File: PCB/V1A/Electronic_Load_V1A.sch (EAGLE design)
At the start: 209 parts, among them IC101 LM50, IC102 LM50, IC301 7805T, IC302 OPA77P, Q101 SIRC10DP, Q102 SIRC10DP, Q103 BC817-16SMD, Q104 BC817-16SMD, Q105 BC807-16SMD, Q106 SIRC10DP, Q107 IXTK102N65X2R+, Q108 SIRC10DP, Q109 SIRC10DP, Q110 SIRC10DP, Q111 IXTK102N65X2R+, Q601 BC807-16SMD, Q602 BC807-16SMD, Q603 BC807-16SMD, Q604 BC807-16SMD, Q605 BC807-16SMD, Q606 BC807-16SMD, Q607 BC807-16SMD, Q608 BC807-16SMD, Q609 BC807-16SMD, Q610 BC807-16SMD, Q611 BC807-16SMD, Q612 BC807-16SMD, U101 AD420, U102 AD420, U103 LT1014I, U104 LTC1865L, U201 AD620, U202 AD620, U203 AD620, U204 AD620, U205 AD620, U206 LTC1865L, U207 LTC1865L, U208 LTC1865L, U301 MAX743, U601 HCPL-063N, U602 HCPL-063N, U603 HCPL-063N, U604 HCPL-063N, U605 HCPL-063N, U606 HCPL-063N

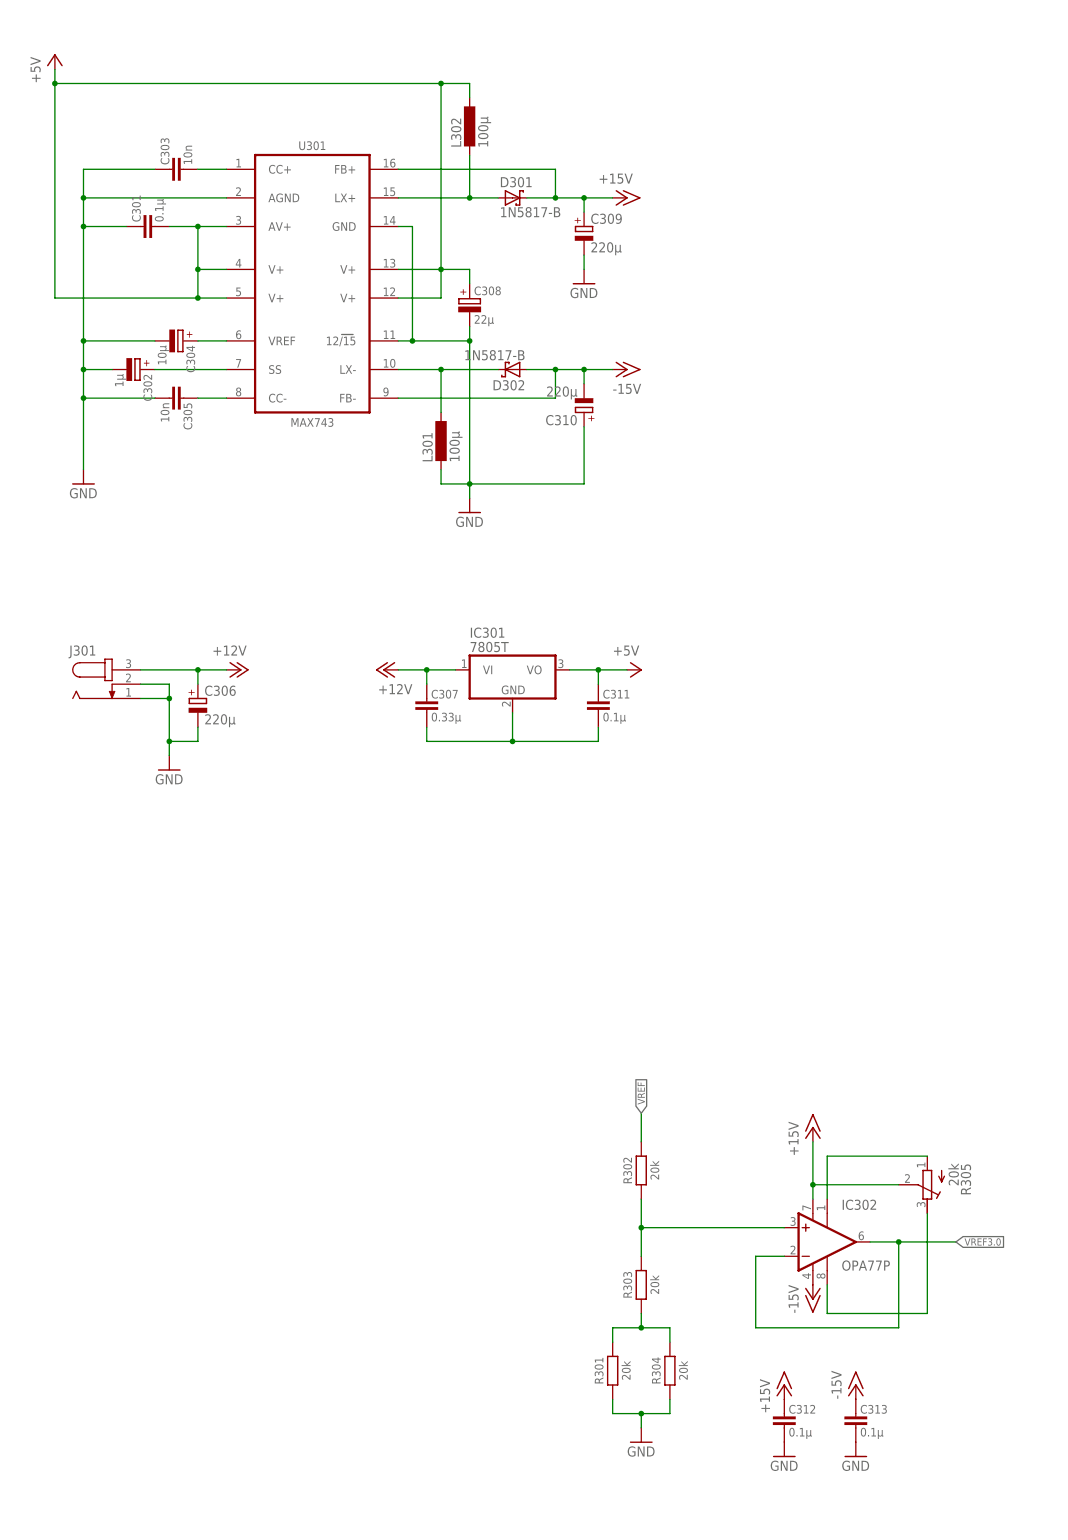
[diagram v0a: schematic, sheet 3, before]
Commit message: ADC/DAC board layout
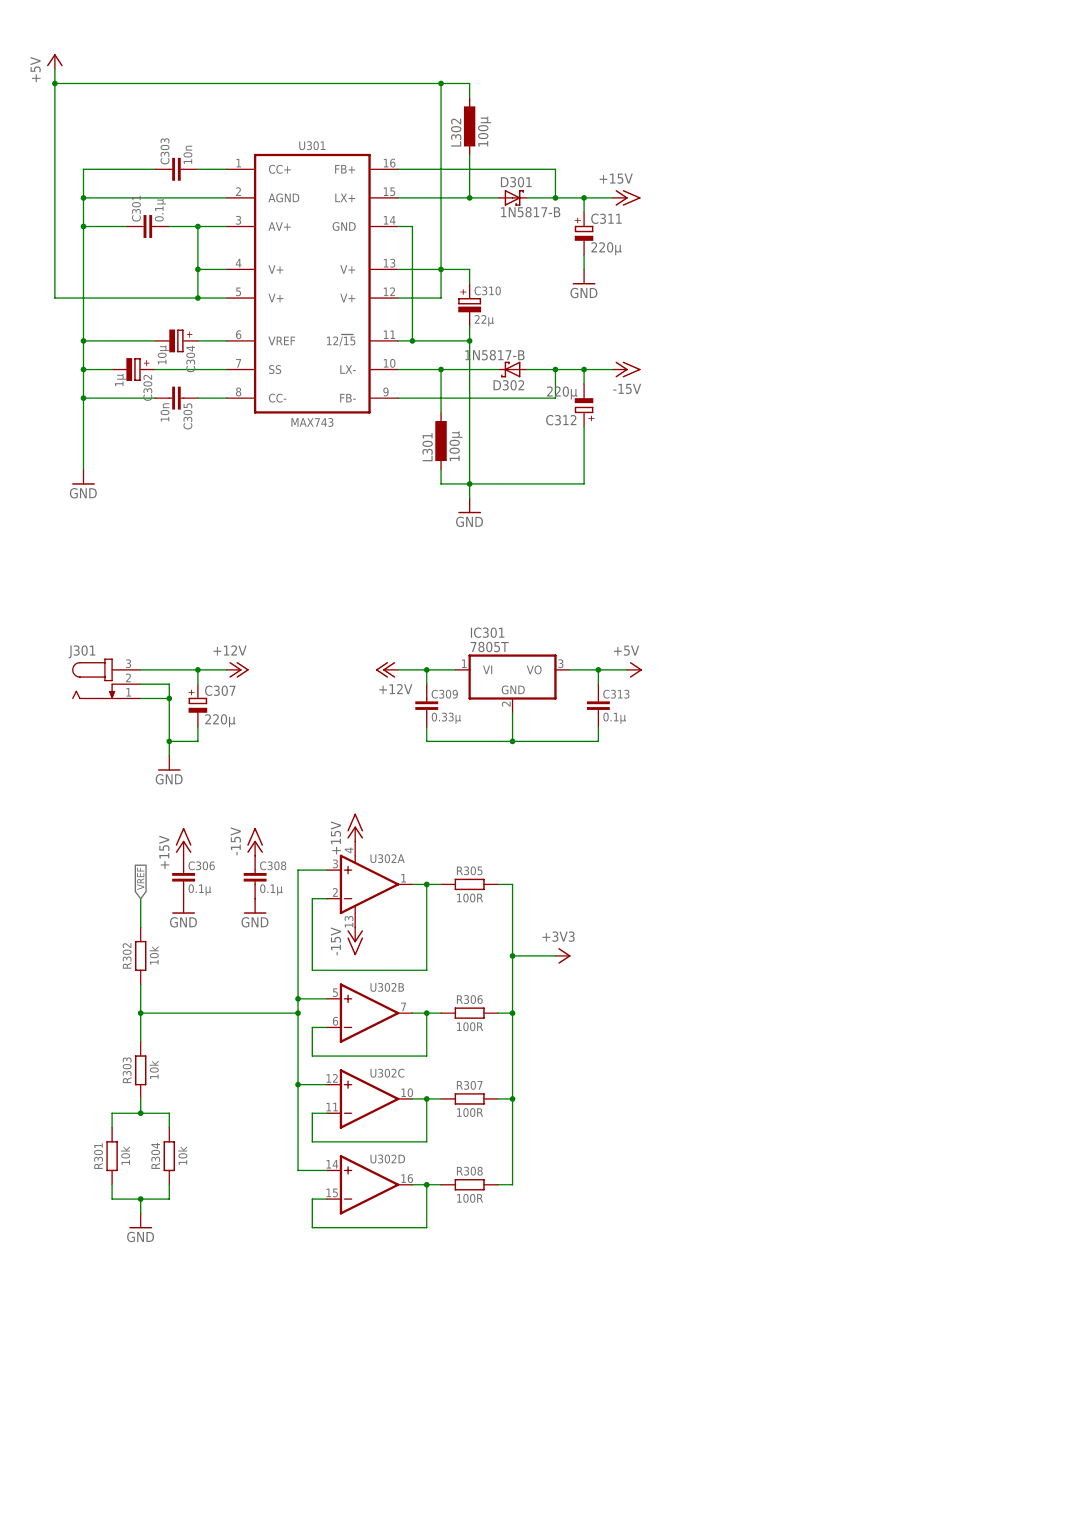
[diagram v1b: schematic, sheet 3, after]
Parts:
- removed IC302: OPA77P, burr-brown:OPA77P
- added R306, R307, R308: 100R, passives:R-EU-3225
- added U302: (no value), ic:LT1014ISW
- C306: value 220µ -> 0.1µ; device rcl:CPOL-EUE3.5-10 -> passives:C-EU-3216
- C307: value 0.33µ -> 220µ; device passives:C-EU-3216 -> rcl:CPOL-EUE3.5-10
- C308: value 22µ -> 0.1µ; device passives:CPOL-6032-C -> passives:C-EU-3216
- C309: value 220µ -> 0.33µ; device rcl:CPOL-EUE3.5-10 -> passives:C-EU-3216
- C310: value 220µ -> 22µ; device rcl:CPOL-EUE3.5-10 -> passives:CPOL-6032-C
- C311, C312: value 0.1µ -> 220µ; device passives:C-EU-3216 -> rcl:CPOL-EUE3.5-10
- R301, R302, R303, R304: value 20k -> 10k
- R305: value 20k -> 100R; device rcl:R-TRIMM4G/J -> passives:R-EU-3225
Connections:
- removed net BYP_G_LOL: Q604.B
- removed net DAC_CLR_ISO: C609.1, R609.1, U603.VO1
- removed net N$78: IC302.+IN, R302.1, R303.2
- removed net N$80: IC302.TRIM2, R305.E
- removed net N$81: IC302.TRIM1, R305.A
- removed net VREF3.0: IC302.-IN, IC302.OUT
- new net BYP: Q603.B
- new net CLR_DAC: Q601.B
- new net N$37: R302.1, R303.2, U302A.+IN, U302B.+IN, U302C.+IN, U302D.+IN
- new net N$38: R306.1, U302B.-IN, U302B.OUT
- new net N$39: R305.1, U302A.-IN, U302A.OUT
- new net N$40: R307.1, U302C.-IN, U302C.OUT
- new net N$43: R308.1, U302D.-IN, U302D.OUT
- net +12V: now also C307.+, C309.1; no longer C306.+, C307.1
- net +15V: now also C306.1, C311.+, U302A.V+; no longer C309.+, C312.1, IC302.V+, R305.S
- net +3V3: now also R305.2, R306.2, R307.2, R308.2
- net +5V: now also C310.+, C313.1; no longer C308.+, C311.1
- net -15V: now also C308.1, C312.-, U302A.V-; no longer C310.-, C313.1, IC302.V-
- net BYP_I: now also C609.1, R609.1, U603.VO1; no longer C610.1, R610.1, U601.VO2
- net CLR_DAC_I: now also C607.1, R607.1, U601.VO1; no longer Q603.B
- net GND: now also C306.2, C307.-, C308.2, C310.-, C311.-, C312.+; no longer C306.-, C308.-, C309.-, C310.+, C312.2, C313.2
- net N$42: now also C309.2, C313.2; no longer C307.2, C311.2
- net SS_DAC: now also Q604.B; no longer Q601.B
- net SS_DAC_I: now also C610.1, R610.1, U601.VO2; no longer C607.1, R607.1, U601.VO1
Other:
- moved on the sheet: C310, C313, R301, R302, R303, R304

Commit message: Board layout
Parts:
- added C314: 0.33µ, passives:C-EU-3216
- added C315: 0.1µ, passives:C-EU-3216
- added IC302: 7805T, linear:7805T
- added PAD1, PAD405: S1, pads:PAD-10X4
- added PAD2, PAD406: S2, pads:PAD-10X4
- added PAD3, PAD407: UUT-, pads:PAD-10X4
- added PAD401: G1, pads:PAD-5X2
- added PAD402: G2, pads:PAD-5X2
- added PAD403: VS+, pads:PAD-5X2
- added PAD404: VS-, pads:PAD-5X2
- added R133, R217: 10k, passives:R-EU-1608
- C107: device rcl:C-EUC1206 -> passives:C-EU-1608
- C121, C122, C209, C210, C211, C212, C216, C607, C608, C609, C610, C611, C612, C619, C620, C621, C622, C623, C624: device passives:C-EU-3216 -> passives:C-EU-1608
- R101, R123, R124, R125, R201, R202, R203, R204, R210, R211, R212, R213, R214, R215, R216, R305, R306, R307, R308: device passives:R-EU-3225 -> passives:R-EU-2012
- R102: value 1k -> 10k; device passives:R-EU-3225 -> passives:R-EU-1608
- R103, R107: value 100R -> 1k; device passives:R-EU-3225 -> passives:R-EU-3216
- R104, R115, R120, R126: value 10k -> 100R; device passives:R-EU-3225 -> passives:R-EU-2012
- R105, R114, R119, R122: value 100R -> 10k; device passives:R-EU-3225 -> passives:R-EU-1608
- R106: value 1k -> 100R; device passives:R-EU-3225 -> passives:R-EU-2012
- R108: value 0R004 -> 100R; device rcl:R-EU_R6332 -> passives:R-EU-2012
- R109, R129: value 2R -> 0R004; device passives:R-EU-3225 -> passives:R-EU-6332
- R110, R130: value 0R004 -> 2R; device rcl:R-EU_R6332 -> passives:R-EU-3216
- R111, R131: value 10k -> 0R004; device passives:R-EU-3225 -> passives:R-EU-6332
- R112, R113, R116, R117, R118, R121, R127, R132, R301, R302, R303, R304, R601, R602, R603, R604, R605, R606, R607, R608, R609, R610, R611, R612, R613, R614, R615, R616, R617, R618, R619, R620, R621, R622, R623, R624: device passives:R-EU-3225 -> passives:R-EU-1608
- R128: value 0R004 -> 10k; device rcl:R-EU_R6332 -> passives:R-EU-1608
- R205, R206, R207, R208, R209: device passives:R-EU-3225 -> passives:R-EU-3216
- U302: value (none) -> LT1014
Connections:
- removed net N$1: Q107.G, R105.2
- removed net N$2: Q111.G, R122.2
- removed net N$36: R205.1, S201.15
- new net GATE1: PAD401.P, Q107.G, R106.2
- new net GATE2: PAD402.P, Q111.G, R123.2
- new net N$44: C314.2, C315.2, IC302.GND
- new net N$45: R217.2, U208.CH1
- new net VSENSE+: PAD403.P, R205.1, S201.15
- net +12V: now also C314.1, IC302.VI, R105.2, R107.2; no longer R104.2, R106.2
- net +5V: now also C315.1, IC302.VO, R102.1
- net BYP_G: now also R104.1, R108.1, R112.2, R115.1, R120.1, R126.1; no longer R103.1, R107.1, R111.2, R114.1, R119.1, R125.1
- net BYP_I: now also R103.1; no longer R102.1
- net CSENSE1_H: now also R109.2, R110.1, R111.2; no longer R108.2, R109.1, R110.2
- net CSENSE1_L: now also PAD1.P, PAD405.P, R110.2, R113.1; no longer R109.2, R112.1
- net CSENSE2_H: now also R129.2, R130.1, R131.2; no longer R128.2, R129.1, R130.2
- net CSENSE2_L: now also PAD2.P, PAD406.P, R114.1, R130.2; no longer R113.1, R129.2
- net FLT_DAC_I: now also R102.2
- net GND: now also R112.1, R133.1, R217.1; no longer R111.1, R131.1
- net LBQ12_G: now also R104.2; no longer R103.2
- net LBQ13_G: now also R108.2; no longer R107.2
- net LBQ21_G: now also R115.2; no longer R114.2
- net LBQ22_G: now also R120.2; no longer R119.2
- net LBQ23_G: now also R126.2; no longer R125.2
- net LQ1_G: now also R106.1, R127.2, R132.2; no longer R105.1, R126.2, R131.2
- net LQ2_G: now also R123.1, R128.2, R133.2; no longer R122.1, R127.2, R132.2
- net N$12: now also R121.2, R127.1; no longer R120.2, R126.1
- net N$13: now also R117.2, R121.1; no longer R115.2, R120.1
- net N$14: now also R113.2, R117.1; no longer R112.2, R115.1
- net N$15: now also R114.2, R119.1; no longer R113.2, R117.1
- net N$16: now also R119.2, R122.1; no longer R117.2, R121.1
- net N$5: now also R107.1; no longer R106.1
- net N$8: now also R103.2, R105.1; no longer R102.2, R104.1
- net N$9: now also R122.2, R128.1; no longer R121.2, R127.1
- net T1_OUT: now also R124.1; no longer R123.1
- net T2_OUT: now also R125.1; no longer R124.1
- net TEMP1: now also R124.2; no longer R123.2
- net TEMP2: now also R125.2; no longer R124.2
- net UUT-: now also PAD3.P, PAD407.P, R109.1, R111.1, R129.1, R131.1; no longer R108.1, R110.1, R128.1, R130.1
- net VSENSE-: now also PAD404.P
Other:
- note added: "External connections"
- moved on the sheet: R102, R103, R104, R105, R106, R107, R108, R109, R110, R111, R112, R113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

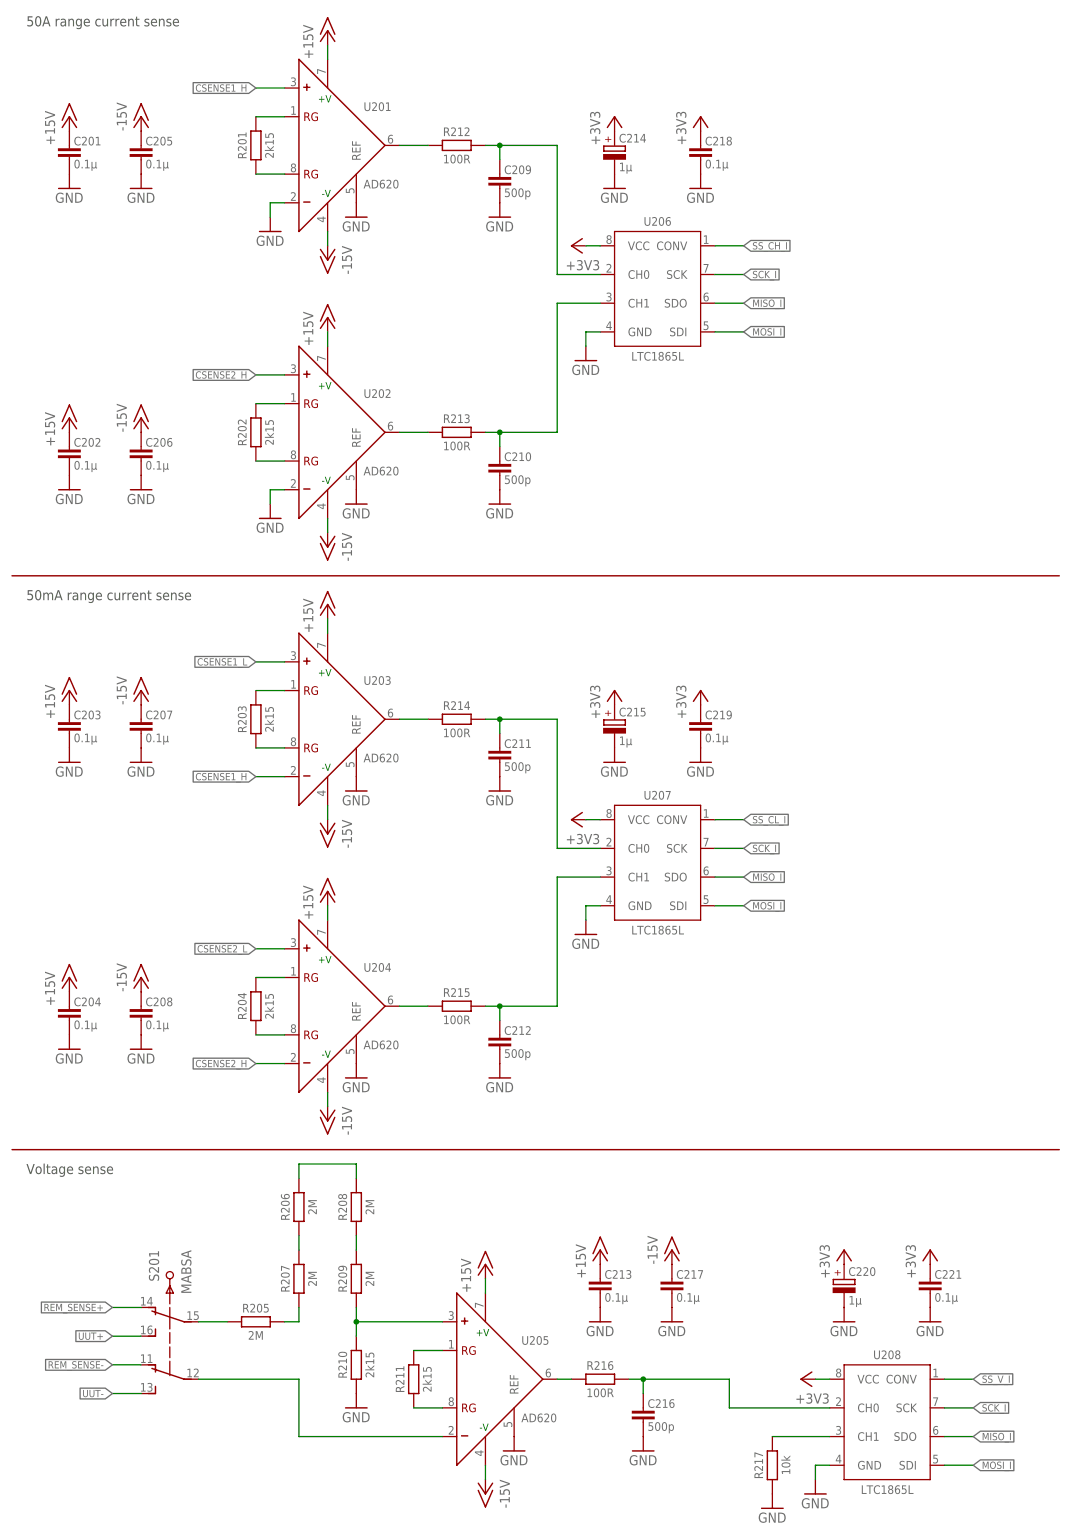
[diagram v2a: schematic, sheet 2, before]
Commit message: Board layout, added remote sense input protection
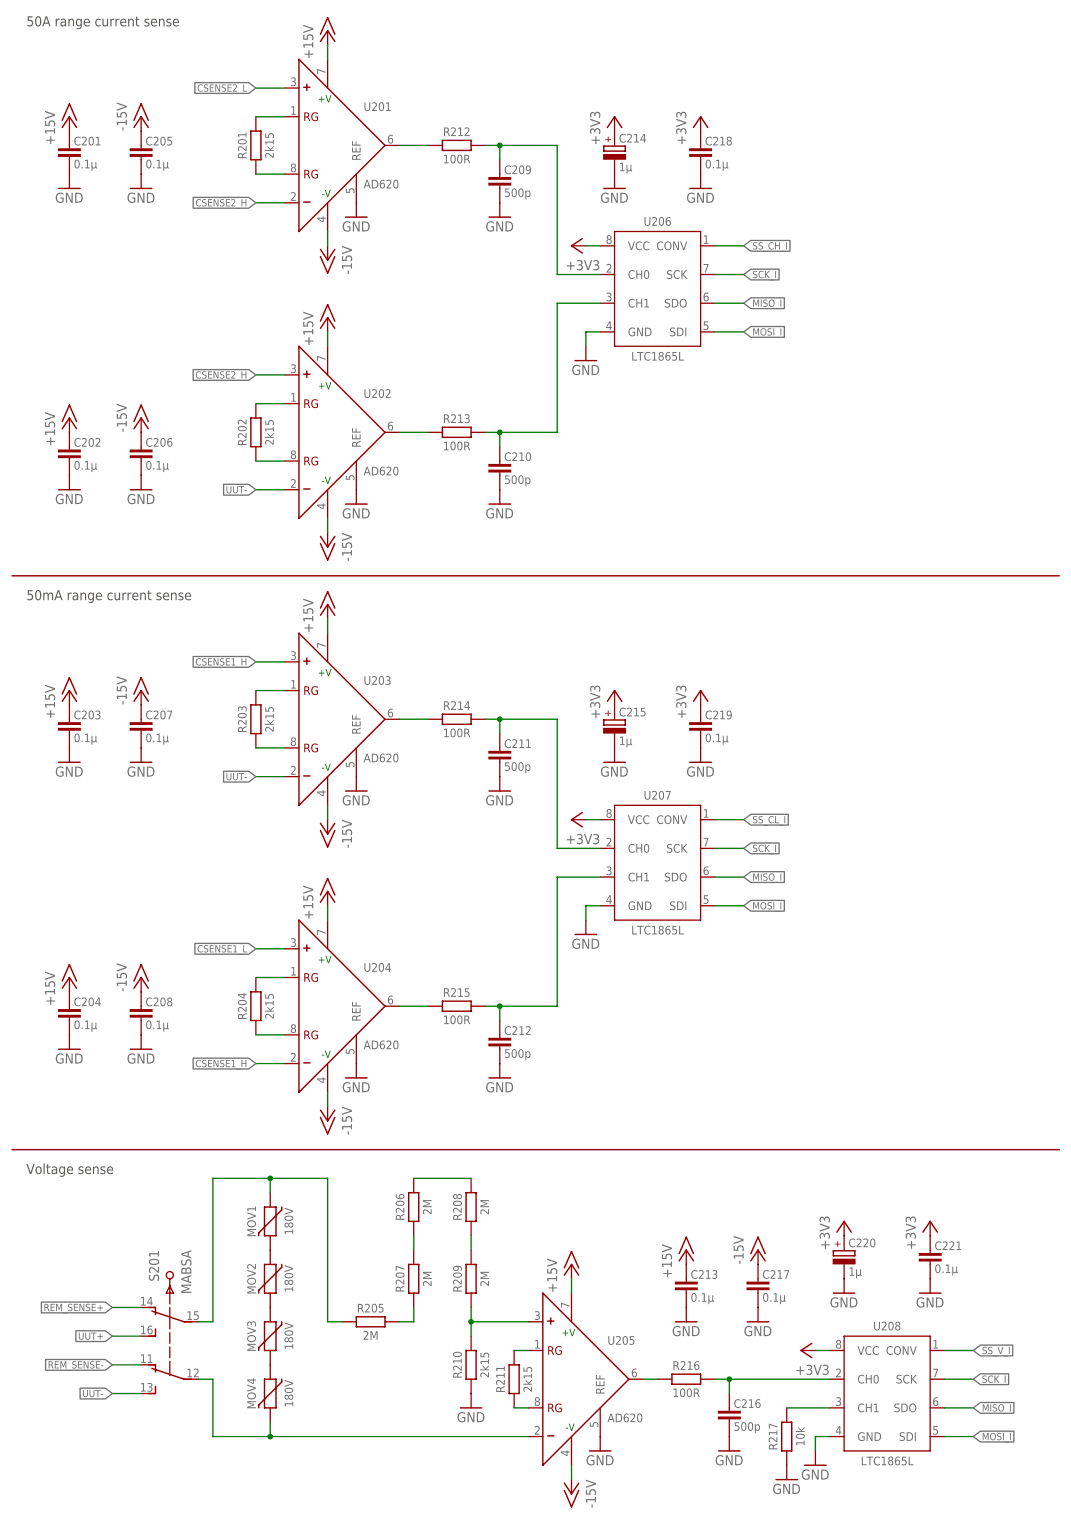
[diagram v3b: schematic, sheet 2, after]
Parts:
- added IC1: MEGA8-AI, atmel:MEGA8-AI
- added MOV1, MOV2, MOV3, MOV4: 180V, passives:MOV-3225
- added PAD4: 12V, pads:PAD-5X2
- added PAD5, PAD9: GND, pads:PAD-5X2
- added PAD6: T1, pads:PAD-5X2
- added PAD7: T2, pads:PAD-5X2
- added PAD8: 5V, pads:PAD-5X2
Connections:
- removed net N$42: C309.2, C313.2, IC301.GND
- removed net N$44: C314.2, C315.2, IC302.GND
- new net N$1: MOV1.2, MOV2.1
- new net N$2: MOV2.2, MOV3.1
- new net N$36: MOV3.2, MOV4.1
- net +12V: now also PAD4.P
- net +5V: now also PAD8.P
- net CSENSE1_H: now also U203.+, U204.-; no longer U201.+, U203.-
- net CSENSE1_L: now also U204.+; no longer U203.+
- net CSENSE2_H: now also U201.-; no longer U204.-
- net CSENSE2_L: now also U201.+; no longer U204.+
- net GND: now also C309.2, C313.2, C314.2, C315.2, IC301.GND, IC302.GND, PAD5.P, PAD9.P; no longer U201.-, U202.-
- net T1_OUT: now also PAD6.P
- net T2_OUT: now also PAD7.P
- net UUT-: now also U202.-, U203.-
- net VSENSE+: now also MOV1.1
- net VSENSE-: now also MOV4.2
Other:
- moved on the sheet: C213, C216, C217, C220, C221, R205, R206, R207, R208, R209, R210, R211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
